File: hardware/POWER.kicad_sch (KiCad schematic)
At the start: 29 parts, among them U501 BQ24210, U601 BQ24210, U701 TPS63070

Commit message: Working on power circuitry layout
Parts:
- L701: footprint (none) -> Inductor_SMD_Wurth:L_Wurth_WE-LQSH-2010
- U501, U601: footprint (none) -> AlfredLib:WSON-10
- U701: footprint (none) -> AlfredLib:VQFN-3.0x2.5
- renumbered CC501 to C501
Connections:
- net GND: now also C601.2, R603.2, R604.2, R605.2, TH601.2, U601.3 (VSS)
- net EN: now reaches R701.2, U701.1 (PS/SYNC), U701.14 (EN)
- net USB_BAT: now reaches R501.1, U501.10 (BAT)
- net SOLAR_ISET: now reaches R604.1, U601.2 (ISET)
- net USB_VDPM: now reaches R505.1, U501.9 (VDPM)
- net SOLAR_BAT: now reaches R601.1, U601.10 (BAT)
- net SOLAR_VTSB: now reaches R602.1, U601.4 (VTSB)
- net SOLAR_TS: now reaches R602.2, TH601.1, U601.5 (TS)
- net SOLAR_EN: now reaches R603.1, U601.7 (~{EN})
- net SOLAR_VDPM: now reaches R605.1, U601.9 (VDPM)
- net L1: now reaches L701.1, U701.11 (L1)
- net VAUX: now reaches C708.1, U701.3 (VAUX)
- net FB: now reaches R702.2, R703.1, U701.5 (FB)
- net L2: now reaches L701.2, U701.9 (L2)
- net USB_VTSB: now reaches R502.1, U501.4 (VTSB)
- net USB_TS: now reaches R502.2, TH501.1, U501.5 (TS)
- net USB_ISET: now reaches R504.1, U501.2 (ISET)
- net USB_EN: now reaches R503.1, U501.7 (~{EN})
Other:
- moved on the sheet: C501, C601, R501, R502, R503, R504, R505, R601, R602, R603, R604, R605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

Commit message: First draft of HW and moved scripts
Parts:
- R503, R603, R701: value 5k1 -> 10k
- R504: value 5k1 -> 511R
- R505: value 5k1 -> 6k8
- R605: value 5k1 -> 0R
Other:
- note added: "0R -> V_min = ~3.65V"
- note added: "3.3 V OUT"
- note added: "511R -> V_min = 4.52"
- note added: "511R -> ~770mA"
- note added: "5k1 -> ~77mA"
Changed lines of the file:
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@@
+		)
+	)
+	(text "3.3 V OUT"
+		(exclude_from_sim no)
+		(at 161.29 110.49 0)
+		(effects
+			(font
+				(size 1.27 1.27)
+			)
+			(justify left)
 		)
 	)
@@
 		)
 	)
+	(text "511R -> ~770mA"
+		(exclude_from_sim no)
+		(at 81.28 77.47 0)
+		(effects
+			(font
+				(size 1.27 1.27)
+			)
+			(justify left)
+		)
+	)
 	(text "POWER CIRCUITRY"
 		(exclude_from_sim no)
 		(at 64.77 95.25 0)
+		(effects
+			(font
+				(size 1.27 1.27)
+			)
+			(justify left)
+		)
+	)
+	(text "0R -> V_min = ~3.65V"
+		(exclude_from_sim no)
+		(at 163.83 80.01 0)
+		(effects
+			(font
+				(size 1.27 1.27)
+			)
+			(justify left)
+		)
+	)
+	(text "511R -> V_min = 4.52"
+		(exclude_from_sim no)
+		(at 81.28 80.01 0)
+		(effects
+			(font
+				(size 1.27 1.27)
+			)
+			(justify left)
+		)
+	)
+	(text "5k1 -> ~77mA"
+		(exclude_from_sim no)
+		(at 163.83 77.47 0)
 		(effects
 			(font
@@
 			)
 		)
-		(property "Value" "5k1"
+		(property "Value" "10k"
 			(at 124.46 119.38 0)
 			(effects
@@
 			)
 		)
-		(property "Value" "5k1"
+		(property "Value" "6k8"
 			(at 97.79 69.85 0)
 			(effects
@@
 			)
 		)
-		(property "Value" "5k1"
+		(property "Value" "0R"
 			(at 180.34 69.85 0)
 			(effects
@@
 			)
 		)
-		(property "Value" "5k1"
+		(property "Value" "511R"
 			(at 90.17 69.85 0)
 			(effects
@@
 			)
 		)
-		(property "Value" "5k1"
+		(property "Value" "10k"
 			(at 82.55 69.85 0)
 			(effects
@@
 			)
 		)
-		(property "Value" "5k1"
+		(property "Value" "10k"
 			(at 165.1 69.85 0)
 			(effects

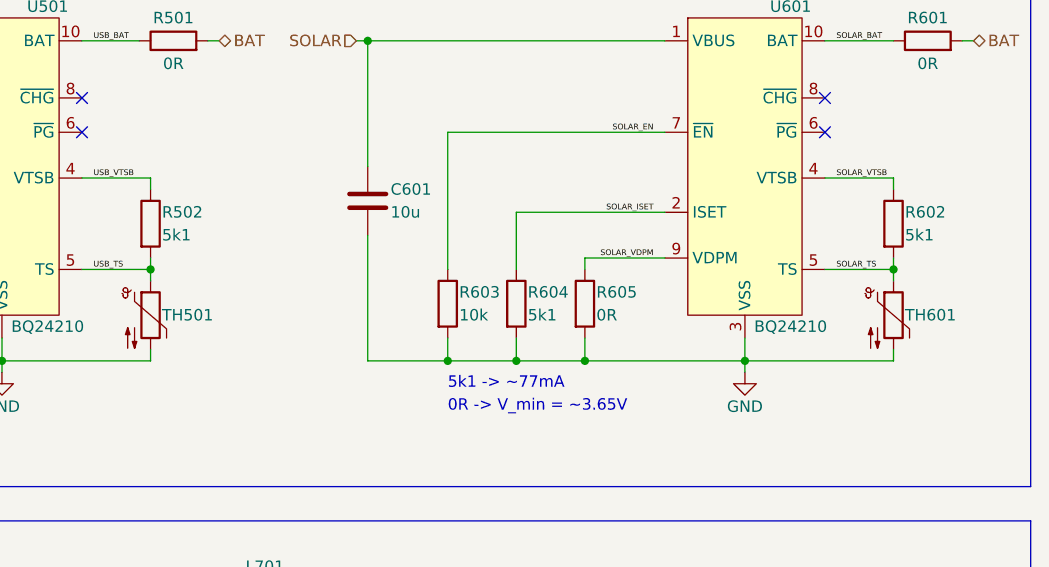
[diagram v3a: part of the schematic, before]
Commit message: Added NTCs
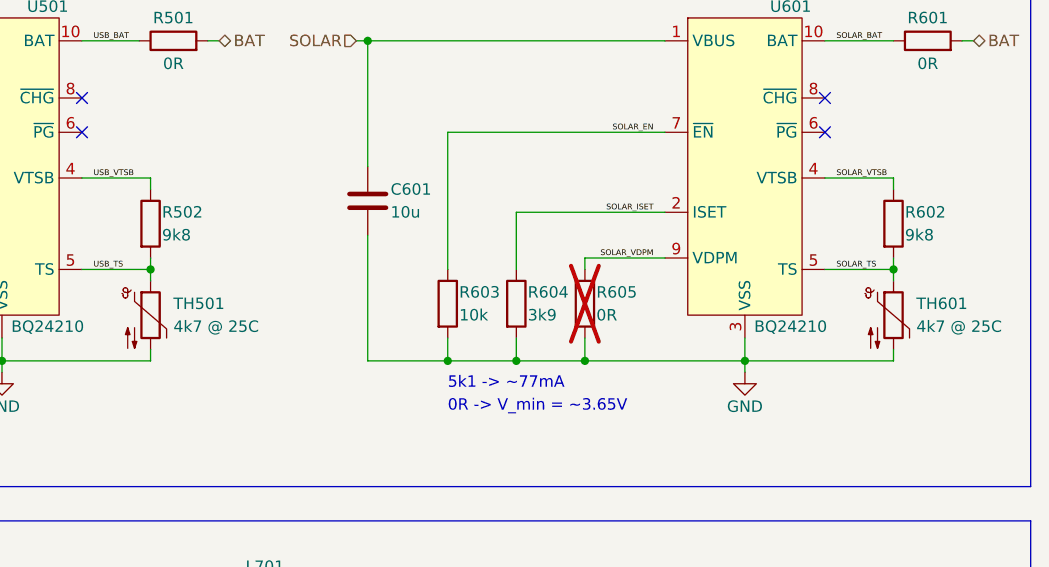
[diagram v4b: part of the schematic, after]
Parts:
- R502, R602: value 5k1 -> 9k8
- R604: value 5k1 -> 3k9
- R605: now not fitted
- TH501, TH601: value Thermistor_NTC -> 4k7 @ 25C; footprint (none) -> Resistor_SMD:R_0603_1608Metric_Pad0.98x0.95mm_HandSolder
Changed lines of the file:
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@@
 			)
 		)
-		(property "Value" "5k1"
+		(property "Value" "3k9"
 			(at 172.72 69.85 0)
 			(effects
@@
 		(dnp no)
 		(property "Reference" "TH601"
-			(at 214.63 69.85 0)
-			(effects
-				(font
-					(size 1.27 1.27)
-				)
-				(justify left)
-			)
-		)
-		(property "Value" "Thermistor_NTC"
-			(at 215.9 71.4374 0)
-			(effects
-				(font
-					(size 1.27 1.27)
-				)
-				(justify left)
-				(hide yes)
-			)
-		)
-		(property "Footprint" ""
+			(at 215.9 68.58 0)
+			(effects
+				(font
+					(size 1.27 1.27)
+				)
+				(justify left)
+			)
+		)
+		(property "Value" "4k7 @ 25C"
+			(at 215.9 71.12 0)
+			(effects
+				(font
+					(size 1.27 1.27)
+				)
+				(justify left)
+			)
+		)
+		(property "Footprint" "Resistor_SMD:R_0603_1608Metric_Pad0.98x0.95mm_HandSolder"
 			(at 213.36 68.58 0)
 			(effects
@@
 		(in_bom yes)
 		(on_board yes)
-		(dnp no)
+		(dnp yes)
 		(property "Reference" "R605"
 			(at 180.34 67.31 0)
@@
 			)
 		)
-		(property "Value" "5k1"
+		(property "Value" "9k8"
 			(at 214.63 60.96 0)
 			(effects
@@
 			)
 		)
-		(property "Value" "5k1"
+		(property "Value" "9k8"
 			(at 132.08 60.96 0)
 			(effects
@@
 		(dnp no)
 		(property "Reference" "TH501"
-			(at 132.08 69.85 0)
-			(effects
-				(font
-					(size 1.27 1.27)
-				)
-				(justify left)
-			)
-		)
-		(property "Value" "Thermistor_NTC"
-			(at 133.35 71.4374 0)
-			(effects
-				(font
-					(size 1.27 1.27)
-				)
-				(justify left)
-				(hide yes)
-			)
-		)
-		(property "Footprint" ""
+			(at 133.35 68.58 0)
+			(effects
+				(font
+					(size 1.27 1.27)
+				)
+				(justify left)
+			)
+		)
+		(property "Value" "4k7 @ 25C"
+			(at 133.35 71.12 0)
+			(effects
+				(font
+					(size 1.27 1.27)
+				)
+				(justify left)
+			)
+		)
+		(property "Footprint" "Resistor_SMD:R_0603_1608Metric_Pad0.98x0.95mm_HandSolder"
 			(at 130.81 68.58 0)
 			(effects
